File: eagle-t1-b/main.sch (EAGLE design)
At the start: 23 parts, among them J1 MOLEX-KK-254-2-HEADER, J2 JST-PH_2-PIN_HEADER, J3 JST-PH_4-PIN_HEADER, J4 JST-PH_2-PIN_HEADER, J5 JST-PH_2-PIN_HEADER, J6 MOLEX-KK-254-2-HEADER, J7 JST-PH_3-PIN_HEADER, J8 JST-PH_3-PIN_HEADER, J9 JST-PH_4-PIN_HEADER, Q1 BS170, U1 POLOLU-TB6612FNG-CARRIER, U2 CD4081BE, U3 POLOLU-MINIMU-9-V3

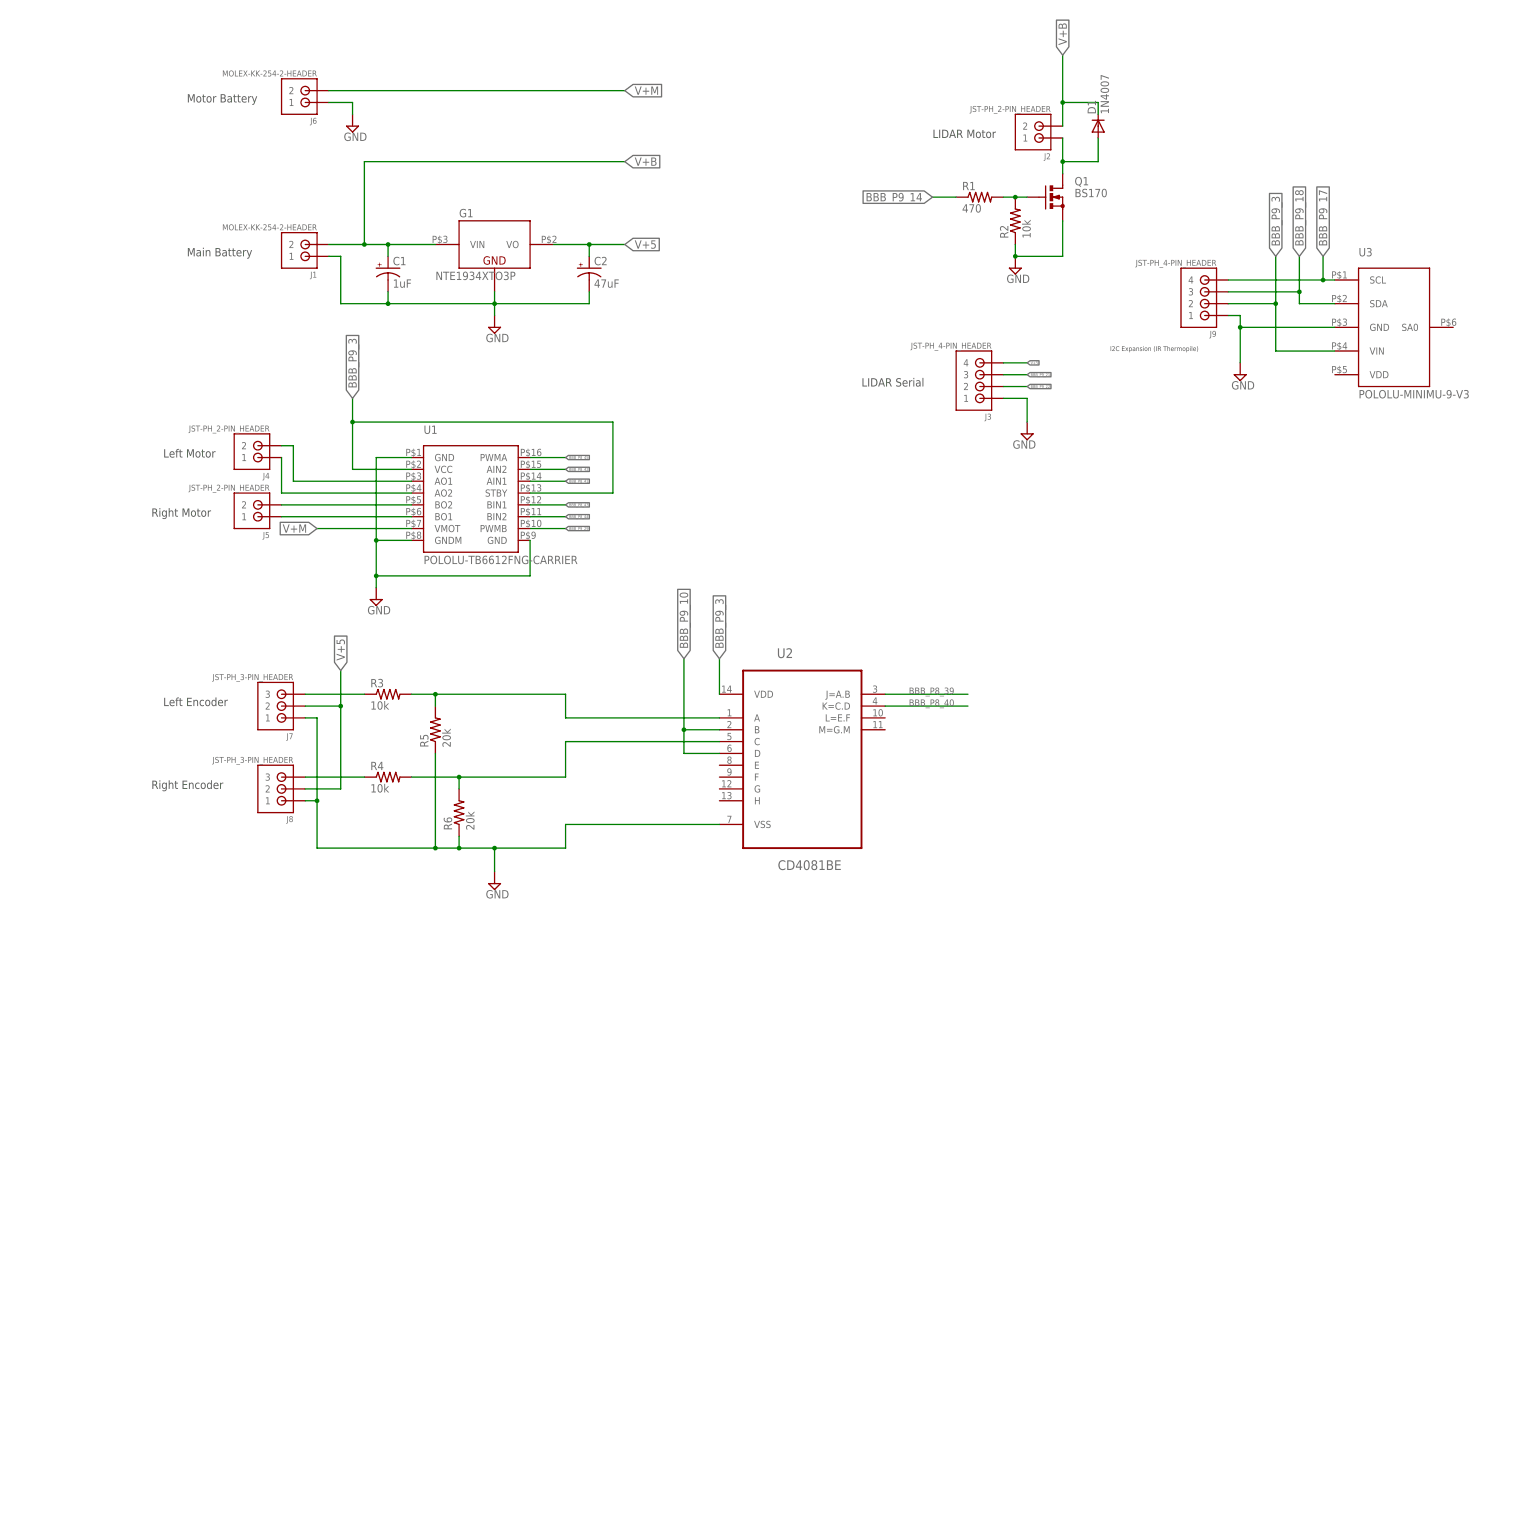
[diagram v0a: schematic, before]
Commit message: Finished main board schematic and pcb layout.
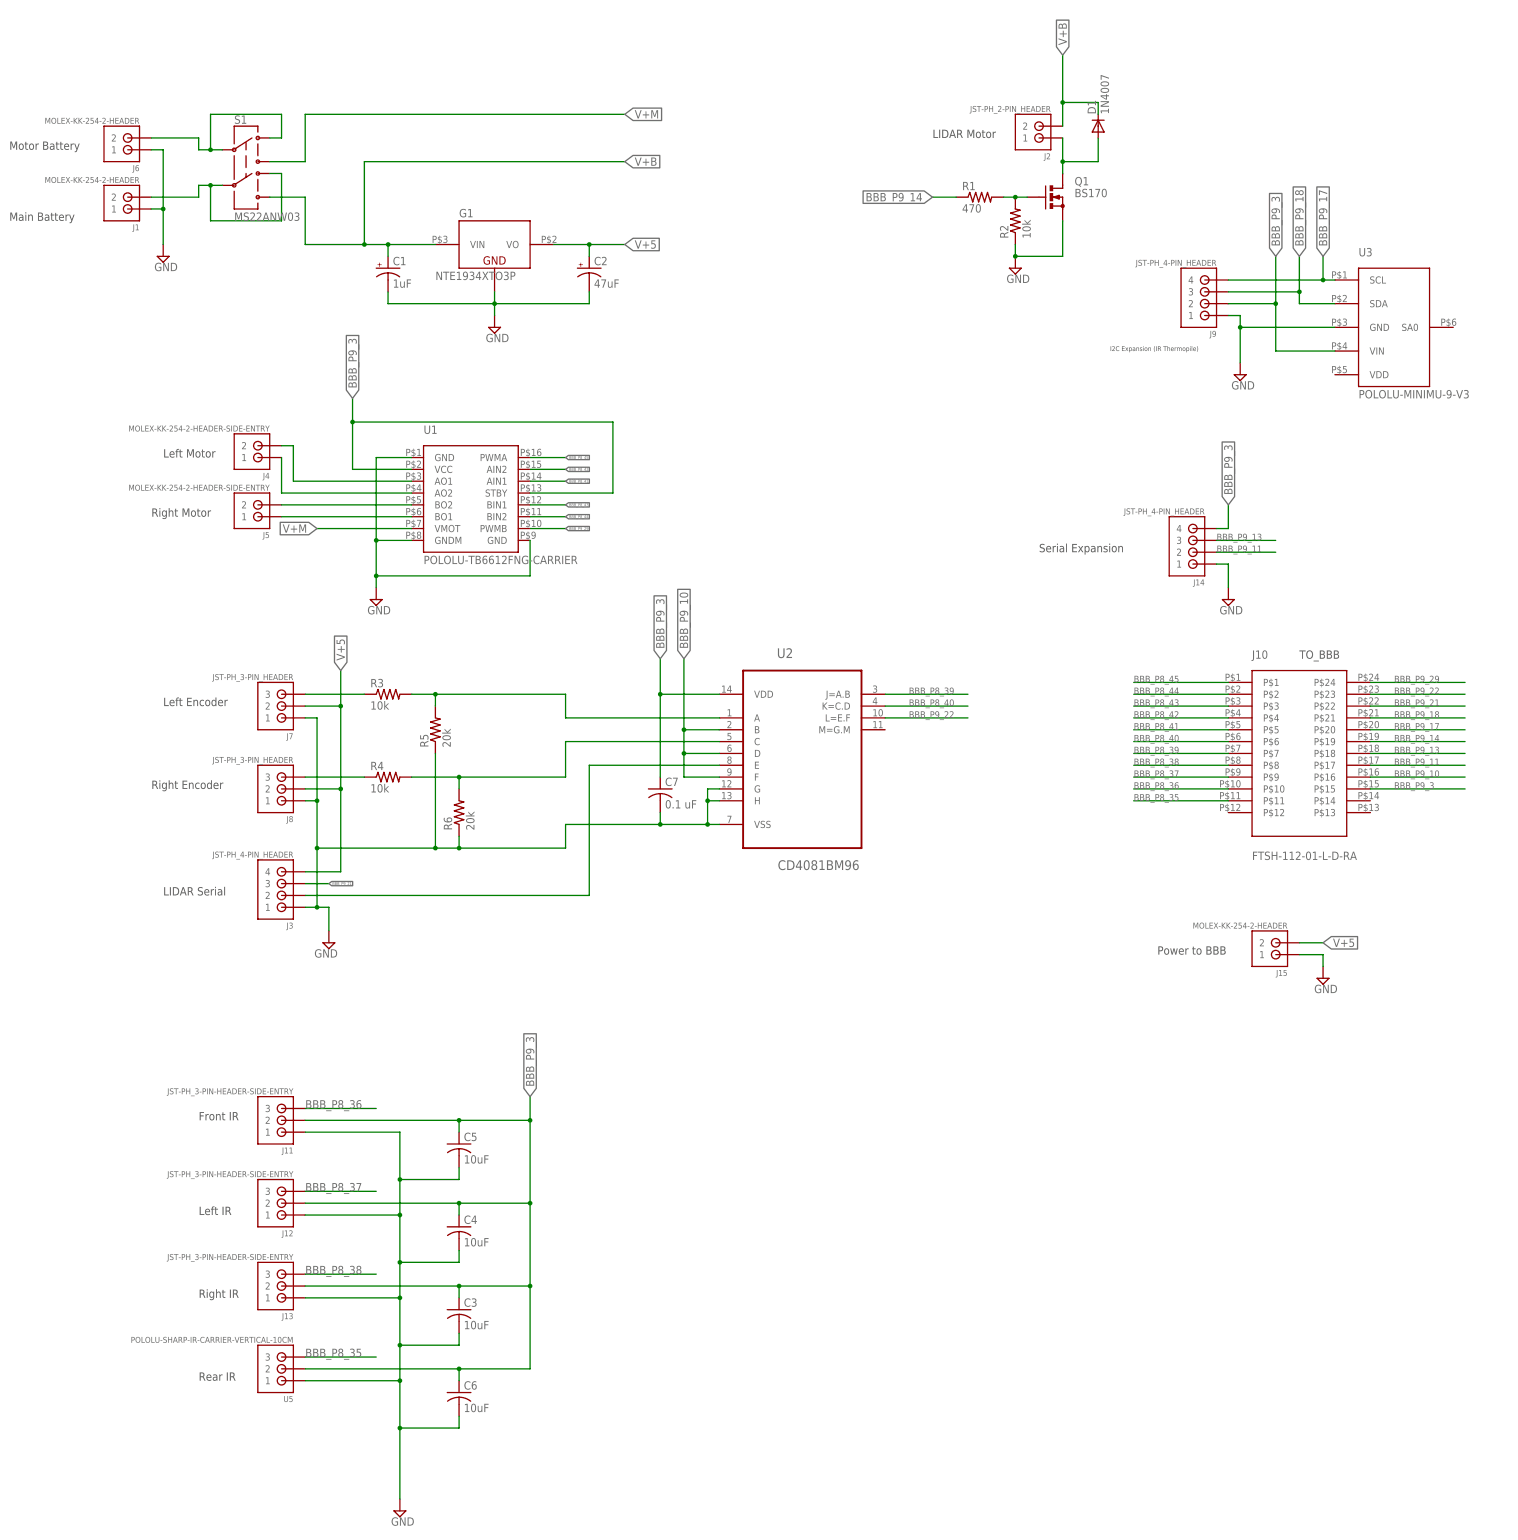
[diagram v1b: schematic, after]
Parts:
- added C3, C4, C5, C6: 10uF, resistor:C-USC0603
- added C7: 0.1 uF, rcl:C-USC0603
- added J10: FTSH-112-01-L-D-RA, custom:FTSH-112-01-L-D-RA
- added J11, J12, J13: JST-PH_3-PIN-HEADER-SIDE-ENTRY, custom:JST-PH_3-PIN-HEADER-SIDE-ENTRY
- added J14: JST-PH_4-PIN_HEADER, SRG:JST-PH_4-PIN_HEADER
- added J15: MOLEX-KK-254-2-HEADER, custom:MOLEX-KK-254-2-HEADER
- added S1: MS22ANW03, custom:SWITCH-DPDT-NKK-MS22ANW03NKK-MS22ANW03
- added U5: POLOLU-SHARP-IR-CARRIER-VERTICAL-10CM, custom:POLOLU-SHARP-IR-CARRIER-VERTICAL-10CM
- C1: device rcl:CPOL-USE1.8-4 -> rcl:CPOL-USB
- C2: device rcl:CPOL-USE2-5 -> rcl:CPOL-USC
- J4, J5: value JST-PH_2-PIN_HEADER -> MOLEX-KK-254-2-HEADER-SIDE-ENTRY; device SRG:JST-PH_2-PIN_HEADER -> custom:MOLEX-KK-254-2-HEADER-SIDE-ENTRY
- R1, R2: device rcl:R-US_0207/10 -> rcl:R-US_R0402
- R3, R4, R5, R6: device resistor:R-US_0207/10 -> resistor:R-US_R0402
- U2: value CD4081BE -> CD4081BM96; device custom:CD4081BE -> custom:CD4081BESO-14
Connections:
- new net BBB_P8_35: J10.P$11, U5.3
- new net BBB_P8_36: J10.P$10, J11.3
- new net BBB_P8_37: J10.P$9, J12.3
- new net BBB_P8_38: J10.P$8, J13.3
- new net BBB_P9_11: J10.P$17, J14.2
- new net BBB_P9_13: J10.P$18, J14.3
- new net N$21: J3.2, U2.E
- new net N$8: J6.2, S1.1, S1.2
- new net N$9: J1.2, S1.4, S1.5
- net BBB_P8_39: now also J10.P$7
- net BBB_P8_40: now also J10.P$6
- net BBB_P8_41: now also J10.P$5
- net BBB_P8_42: now also J10.P$4
- net BBB_P8_43: now also J10.P$3
- net BBB_P8_44: now also J10.P$2
- net BBB_P8_45: now also J10.P$1
- net BBB_P9_10: now also J10.P$16, U2.F
- net BBB_P9_14: now also J10.P$19
- net BBB_P9_17: now also J10.P$20
- net BBB_P9_18: now also J10.P$21
- net BBB_P9_21: now also J10.P$22
- net BBB_P9_22: now also J10.P$23, U2.L=E.F; no longer J3.2
- net BBB_P9_29: now also J10.P$24
- net BBB_P9_3: now also C3.1, C4.1, C5.1, C6.1, C7.1, J10.P$15, J11.2, J12.2, J13.2, J14.4, U5.2
- net GND: now also C3.2, C4.2, C5.2, C6.2, C7.2, J11.1, J12.1, J13.1, J14.1, J15.1, U2.G, U2.H, U5.1
- net V+5: now also J15.2
- net V+B: now also S1.6
- net V+M: now also S1.3; no longer J6.2
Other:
- note added: "Front IR"
- note added: "Left IR"
- note added: "Power to BBB"
- note added: "Rear IR"
- note added: "Right IR"
- note added: "Serial Expansion"
- note added: "TO_BBB"
- moved on the sheet: J1, J3, J6

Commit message: Finalized circuit board designs.
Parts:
- J10: device custom:FTSH-112-01-L-D-RA -> custom:FTSH-112-CONNRIGHT-ANGLE
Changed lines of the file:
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@@
 <part name="SUPPLY7" library="supply2" deviceset="GND" device=""/>
 <part name="J9" library="SRG" deviceset="JST-PH_4-PIN_HEADER" device=""/>
-<part name="J10" library="custom" deviceset="FTSH-112-01-L-D-RA" device="" value="FTSH-112-01-L-D-RA"/>
+<part name="J10" library="custom" deviceset="FTSH-112-CONN" device="RIGHT-ANGLE" value="FTSH-112-01-L-D-RA"/>
 <part name="SUPPLY8" library="supply2" deviceset="GND" device=""/>
 <part name="C3" library="resistor" deviceset="C-US" device="C0603" value="10uF"/>
